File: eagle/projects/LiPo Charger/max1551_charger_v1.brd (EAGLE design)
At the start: 100 x 80 mm, 5 parts

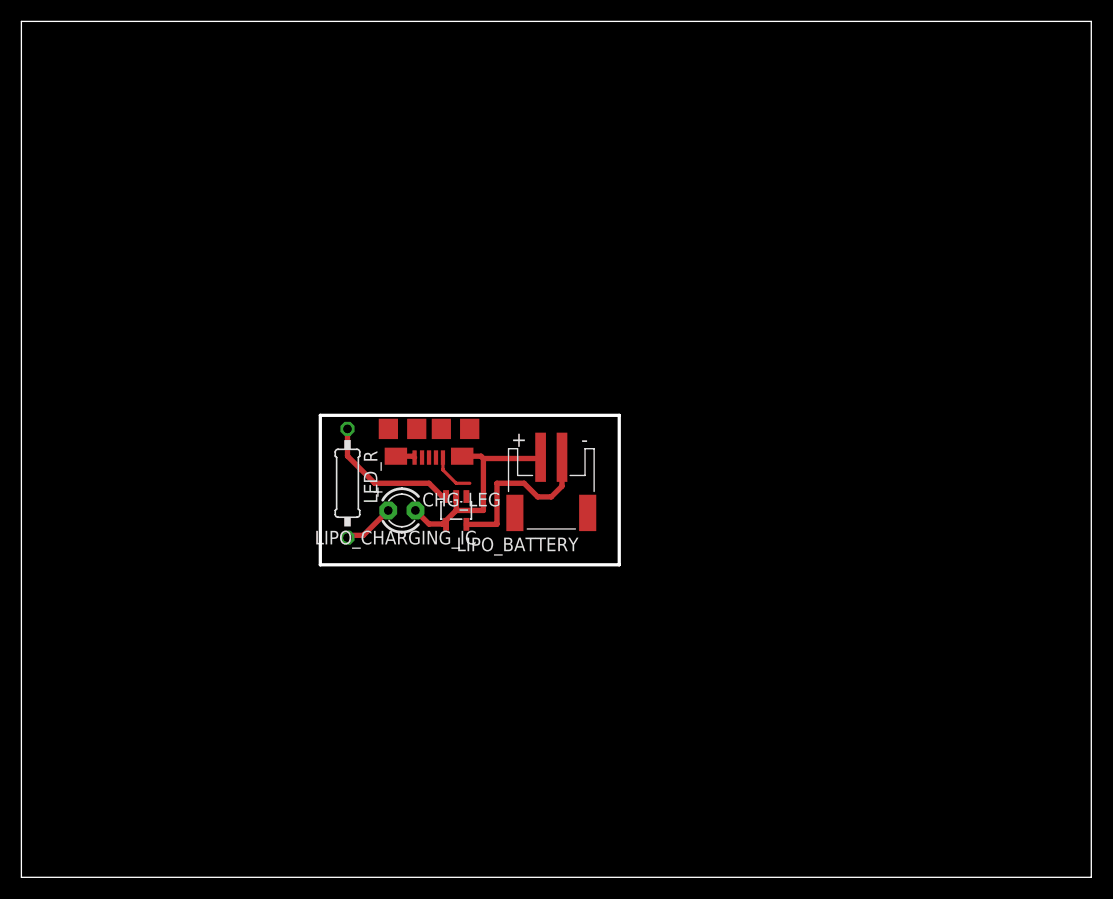
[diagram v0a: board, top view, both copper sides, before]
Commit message: Update LiPo Charger with MAX 1551
This board was printed and tested and it seems to work.

It's a bit simple/slow though so a better charger circuit
would probably be advantageous in the future.  Plus the
MAX1551 charger ICs are expensive ~$2 each.

However, it works!  So I'm saving these designs for later

Signed-off-by: Rave Strapon <ravestrapon@gmail.com>
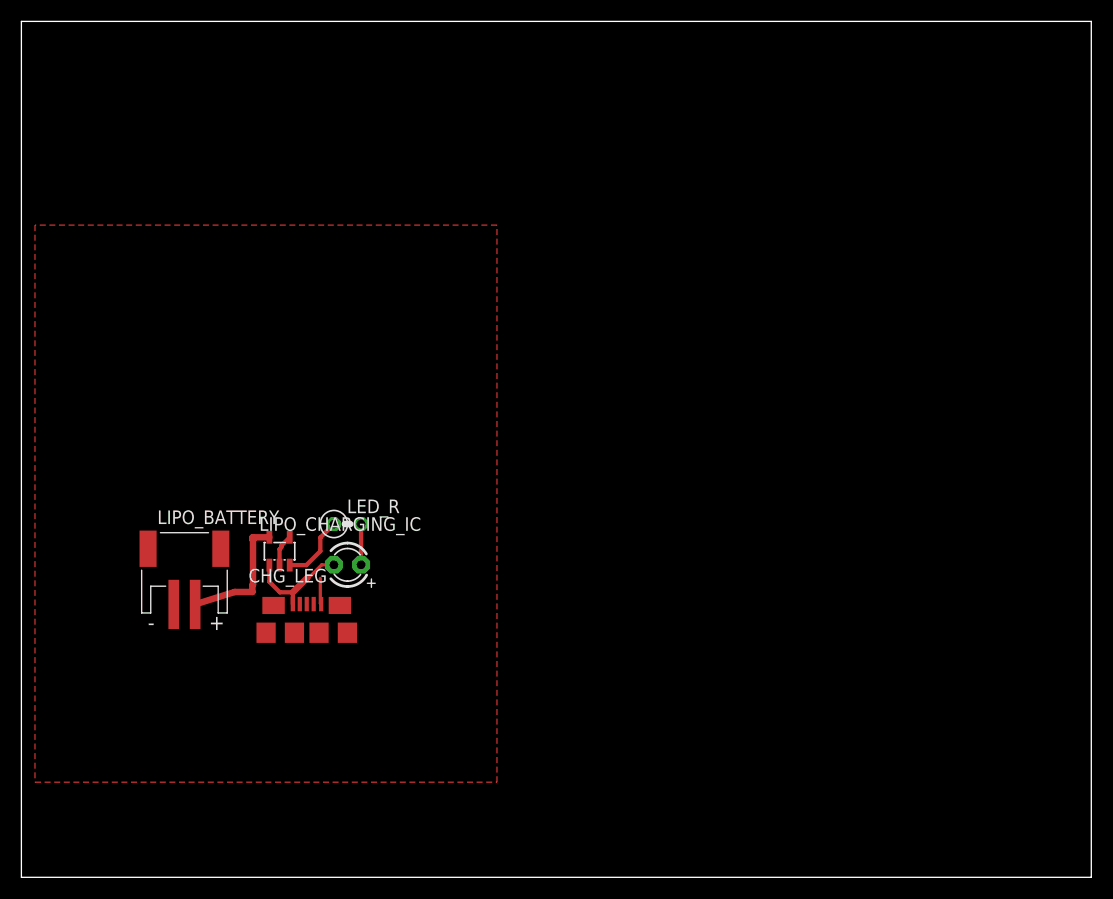
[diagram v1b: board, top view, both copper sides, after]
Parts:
- LED_R: device rcl:0207/10 -> rcl:0207/2V
- USB_JACK: device cmooney:FCI-10118192-0001LF -> ravestrapon:FCI-10118192-0001LF
- moved LIPO_BATTERY 34.9 mm to (15.2, 29.2), turned to 0 degrees
- moved USB_JACK 22.2 mm to (26.7, 22.9), turned to 0 degrees
- moved LIPO_CHARGING_IC 16.9 mm to (24.1, 30.5), turned to 0 degrees
- moved CHG_LEG 7.18 mm to (30.5, 29.2), turned to 180 degrees
- moved LED_R 3.81 mm to (30.5, 33.0), turned to 0 degrees
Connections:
- removed net N$2: CHG_LEG.K, LIPO_BATTERY.1, LIPO_CHARGING_IC.2, LIPO_CHARGING_IC.4, USB_JACK.GND@1, USB_JACK.GND@2, USB_JACK.GND@3, USB_JACK.GND@4, USB_JACK.GND@5, USB_JACK.GND@6, USB_JACK.GND@7
- new net GND: LIPO_BATTERY.2, LIPO_CHARGING_IC.2, LIPO_CHARGING_IC.4, USB_JACK.GND
- net BAT_POS: now also LIPO_BATTERY.1; no longer LIPO_BATTERY.2
- net USB_POWER: now also CHG_LEG.K
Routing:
- net N$2: track 22.8 -> 0.00 mm
- net CHG_INDICATOR: track 13.3 -> 6.46 mm
- net USB_POWER: track 4.23 -> 10.2 mm
- net GND: track 0.00 -> 5.43 mm
- net BAT_POS: track 16.4 -> 12.3 mm
- net N$1: track 4.87 -> 3.81 mm
- added copper zone on layer 1, net GND
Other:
- outline, holes or cut-outs redrawn
